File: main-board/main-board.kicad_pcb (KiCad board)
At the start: 4 copper layers, 142.9 x 86.4 mm, 177 parts, among them J1 BOOT, J10 8P8CDouble, J11 Qwiic, J12 Qwiic, J13 Qwiic, J14 YELLOW, J15 GREEN, J2 USB Header, J3 JTAG, J4 5V Input, J5 StatusPanel, J6 Magjack, J7 8P8CDouble, J8 8P8CDouble, J9 8P8CDouble, Q1 N Channel, Q10 N Channel, Q11 N Channel, Q12 N Channel, Q13 P Channel, Q14 P Channel, Q15 P Channel, Q16 P Channel, Q17 P Channel, Q2 N Channel, Q3 N Channel, Q4 N Channel, Q5 P Channel, Q6 P Channel, Q7 P Channel, Q8 P Channel, Q9 N Channel, U1 STM32H743ZITx, U10 ISL83490, U11 ISL83490, U12 ISL83490, U13 W25Q80DVSNIG, U2 USBLC6-2SC6, U3 3.3V Reg, U4 KSZ8041MLL, U5 ISL83490, U6 ISL83490, U7 ISL83490, U8 ISL83490, U9 ISL83490, X1 20MHz Oscillator, X2 25MHz Oscillator

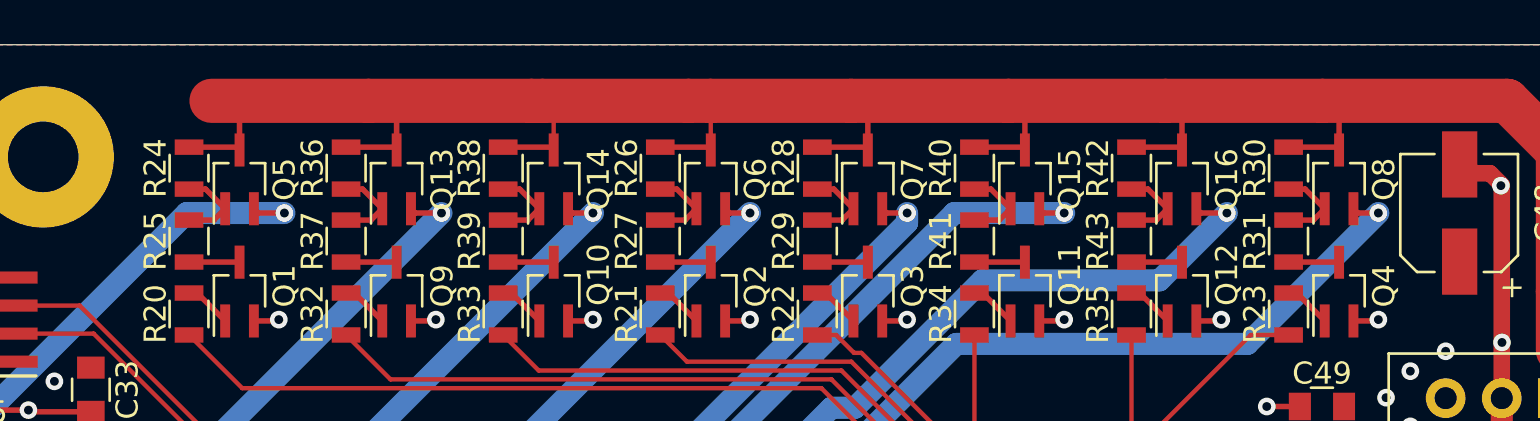
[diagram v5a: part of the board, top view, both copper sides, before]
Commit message: Had the p-channel FETs in the wrong orientation, and an unnecessary resistor.
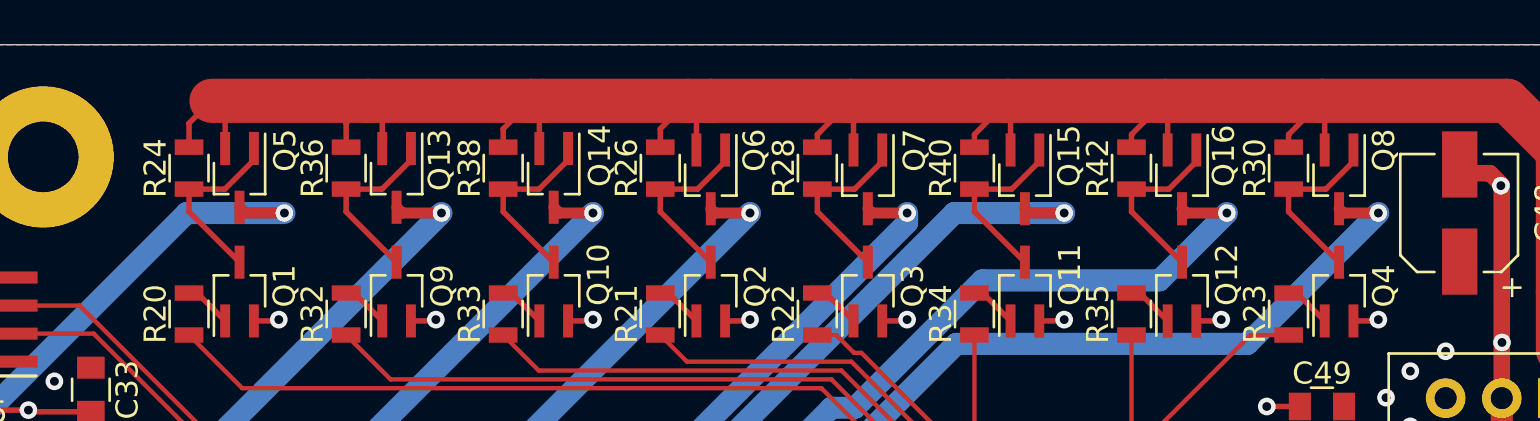
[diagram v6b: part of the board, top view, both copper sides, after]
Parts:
- removed R25, R27, R29, R31, R37, R39, R41, R43: 100, Resistors_SMD:R_0805
- R24, R26, R28, R30, R36, R38, R40, R42: value 10k -> 4700
- moved Q13 0.07 mm to (130.3, 51.8), turned to 270 degrees
- moved Q14 0.07 mm to (137.4, 51.8), turned to 270 degrees
- moved Q5 0.07 mm to (123.2, 51.8), turned to 270 degrees
- turned Q15 to 270 degrees
- turned Q16 to 270 degrees
- turned Q6 to 270 degrees
- turned Q7 to 270 degrees
- turned Q8 to 270 degrees
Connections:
- Q13 pad 2: Net-(C54-Pad1) -> +5V
- Q13 pad 3: +5V -> Net-(C54-Pad1)
- Q14 pad 1: Net-(Q14-Pad1) -> Net-(Q10-Pad3)
- Q14 pad 2: Net-(C55-Pad1) -> +5V
- Q14 pad 3: +5V -> Net-(C55-Pad1)
- Q15 pad 1: Net-(Q15-Pad1) -> Net-(Q11-Pad3)
- Q15 pad 2: Net-(C56-Pad1) -> +5V
- Q15 pad 3: +5V -> Net-(C56-Pad1)
- Q16 pad 1: Net-(Q16-Pad1) -> Net-(Q12-Pad3)
- Q16 pad 2: Net-(C57-Pad1) -> +5V
- Q16 pad 3: +5V -> Net-(C57-Pad1)
- Q5 pad 1: Net-(Q5-Pad1) -> Net-(Q1-Pad3)
- Q5 pad 2: Net-(C50-Pad1) -> +5V
- Q5 pad 3: +5V -> Net-(C50-Pad1)
- Q6 pad 1: Net-(Q6-Pad1) -> Net-(Q2-Pad3)
- Q6 pad 2: Net-(C51-Pad1) -> +5V
- Q6 pad 3: +5V -> Net-(C51-Pad1)
- Q7 pad 1: Net-(Q7-Pad1) -> Net-(Q3-Pad3)
- Q7 pad 2: Net-(C52-Pad1) -> +5V
- Q7 pad 3: +5V -> Net-(C52-Pad1)
- Q8 pad 1: Net-(Q8-Pad1) -> Net-(Q4-Pad3)
- Q8 pad 2: Net-(C53-Pad1) -> +5V
- Q8 pad 3: +5V -> Net-(C53-Pad1)
- Q9 pad 3: Net-(Q9-Pad3) -> Net-(Q13-Pad1)
- R24 pad 2: Net-(Q5-Pad1) -> Net-(Q1-Pad3)
- R26 pad 2: Net-(Q6-Pad1) -> Net-(Q2-Pad3)
- R28 pad 2: Net-(Q7-Pad1) -> Net-(Q3-Pad3)
- R30 pad 2: Net-(Q8-Pad1) -> Net-(Q4-Pad3)
- R38 pad 2: Net-(Q14-Pad1) -> Net-(Q10-Pad3)
- R40 pad 2: Net-(Q15-Pad1) -> Net-(Q11-Pad3)
- R42 pad 2: Net-(Q16-Pad1) -> Net-(Q12-Pad3)
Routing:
- net Net-(Q1-Pad3): track 2.29 -> 8.27 mm
- net Net-(Q10-Pad3): track 2.29 -> 8.26 mm
- net Net-(Q4-Pad3): track 2.29 -> 8.23 mm
- net Net-(Q3-Pad3): track 2.29 -> 8.23 mm
- net Net-(Q12-Pad3): track 2.29 -> 8.23 mm
- net Net-(Q11-Pad3): track 2.29 -> 8.23 mm
- net Net-(Q2-Pad3): track 2.29 -> 8.23 mm
- net +5V: track 130.0 -> 135.4 mm
- net Net-(Q13-Pad1): track 3.85 -> 8.26 mm
- net Net-(Q8-Pad1): track 3.85 -> 0.00 mm
- net Net-(Q14-Pad1): track 3.85 -> 0.00 mm
- net Net-(Q5-Pad1): track 3.85 -> 0.00 mm
- net Net-(Q16-Pad1): track 3.85 -> 0.00 mm
- net Net-(Q15-Pad1): track 3.85 -> 0.00 mm
- net Net-(Q6-Pad1): track 3.85 -> 0.00 mm
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
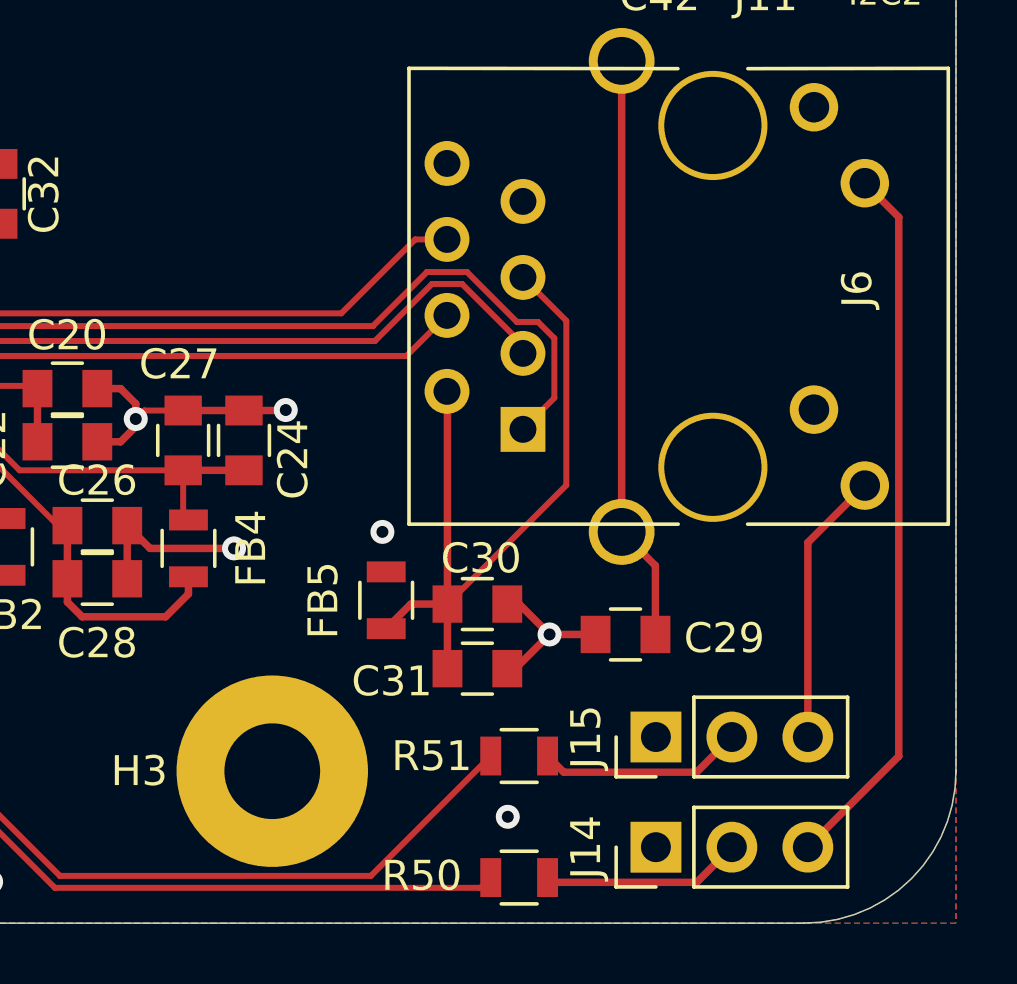
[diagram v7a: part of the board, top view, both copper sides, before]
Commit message: Moved ethernet LEDs to a single 2x3 header instead of two 1x3
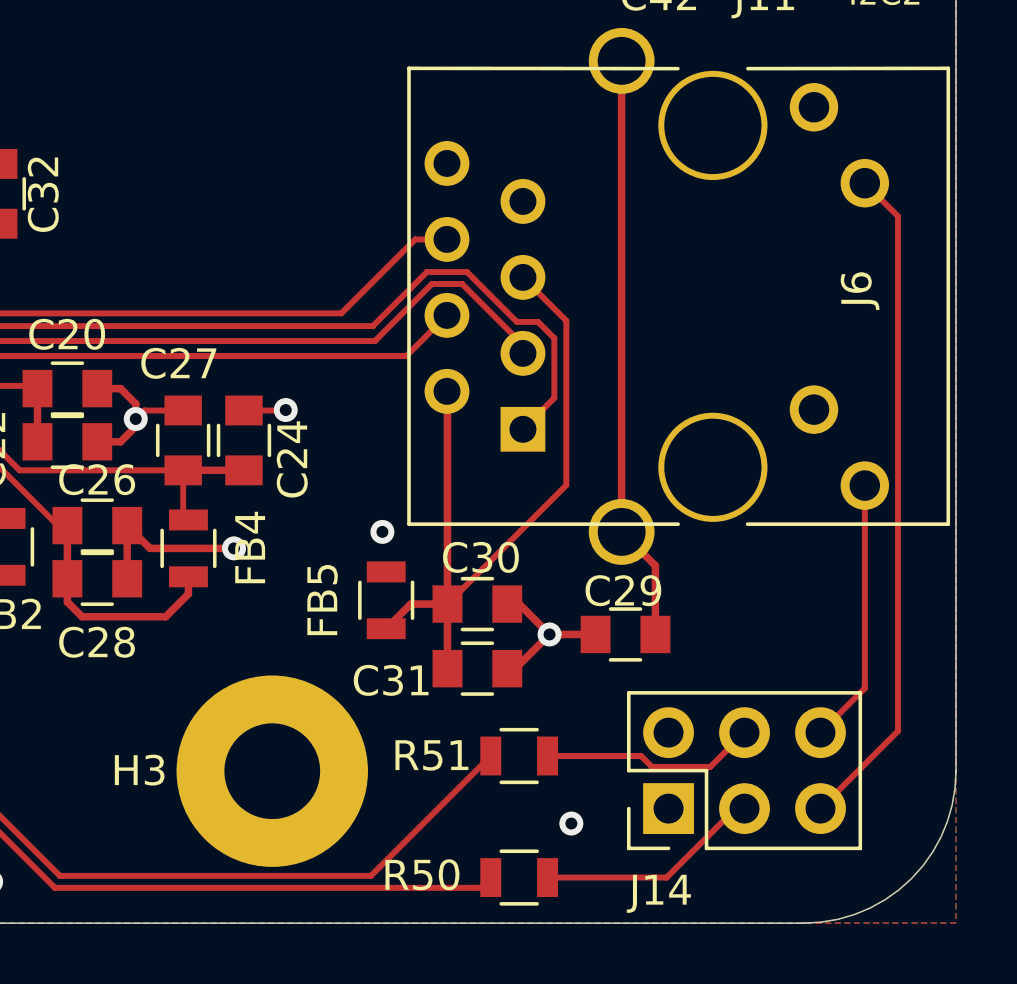
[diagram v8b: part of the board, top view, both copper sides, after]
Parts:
- removed J15: GREEN, Pin_Headers:Pin_Header_Straight_1x03_Pitch2.54mm
- J14: value YELLOW -> EthernetLEDs; footprint Pin_Headers:Pin_Header_Straight_1x03_Pitch2.54mm -> Pin_Headers:Pin_Header_Straight_2x03_Pitch2.54mm
- moved J14 1.36 mm to (203.8, 128.2)
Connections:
- J14 pad 2: Net-(J14-Pad2) -> +3V3
- J14 pad 3: /JACK_YEL_CATH -> Net-(J14-Pad3)
- R50 pad 2: Net-(J14-Pad2) -> Net-(J14-Pad3)
- R51 pad 2: Net-(J15-Pad2) -> Net-(J14-Pad4)
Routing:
- net Net-(J14-Pad3): track 0.00 -> 7.77 mm
- net Net-(J14-Pad4): track 0.00 -> 7.21 mm
- net Net-(J15-Pad2): track 6.87 -> 0.00 mm
- net Net-(J14-Pad2): track 6.71 -> 0.00 mm
- net GND: track 318.2 -> 316.2 mm
- net /JACK_YEL_CATH: track 23.9 -> 22.4 mm
